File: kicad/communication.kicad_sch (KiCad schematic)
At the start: 51 parts, among them J1 CAN1A, J2 CAN1B, J3 Conn_01x02_Socket, J6 CAN1A, J7 CAN1B, U13 SK9822-EC20, U15 TJA1462ATK, U8 TJA1462ATK, U9 TJA1103AHN

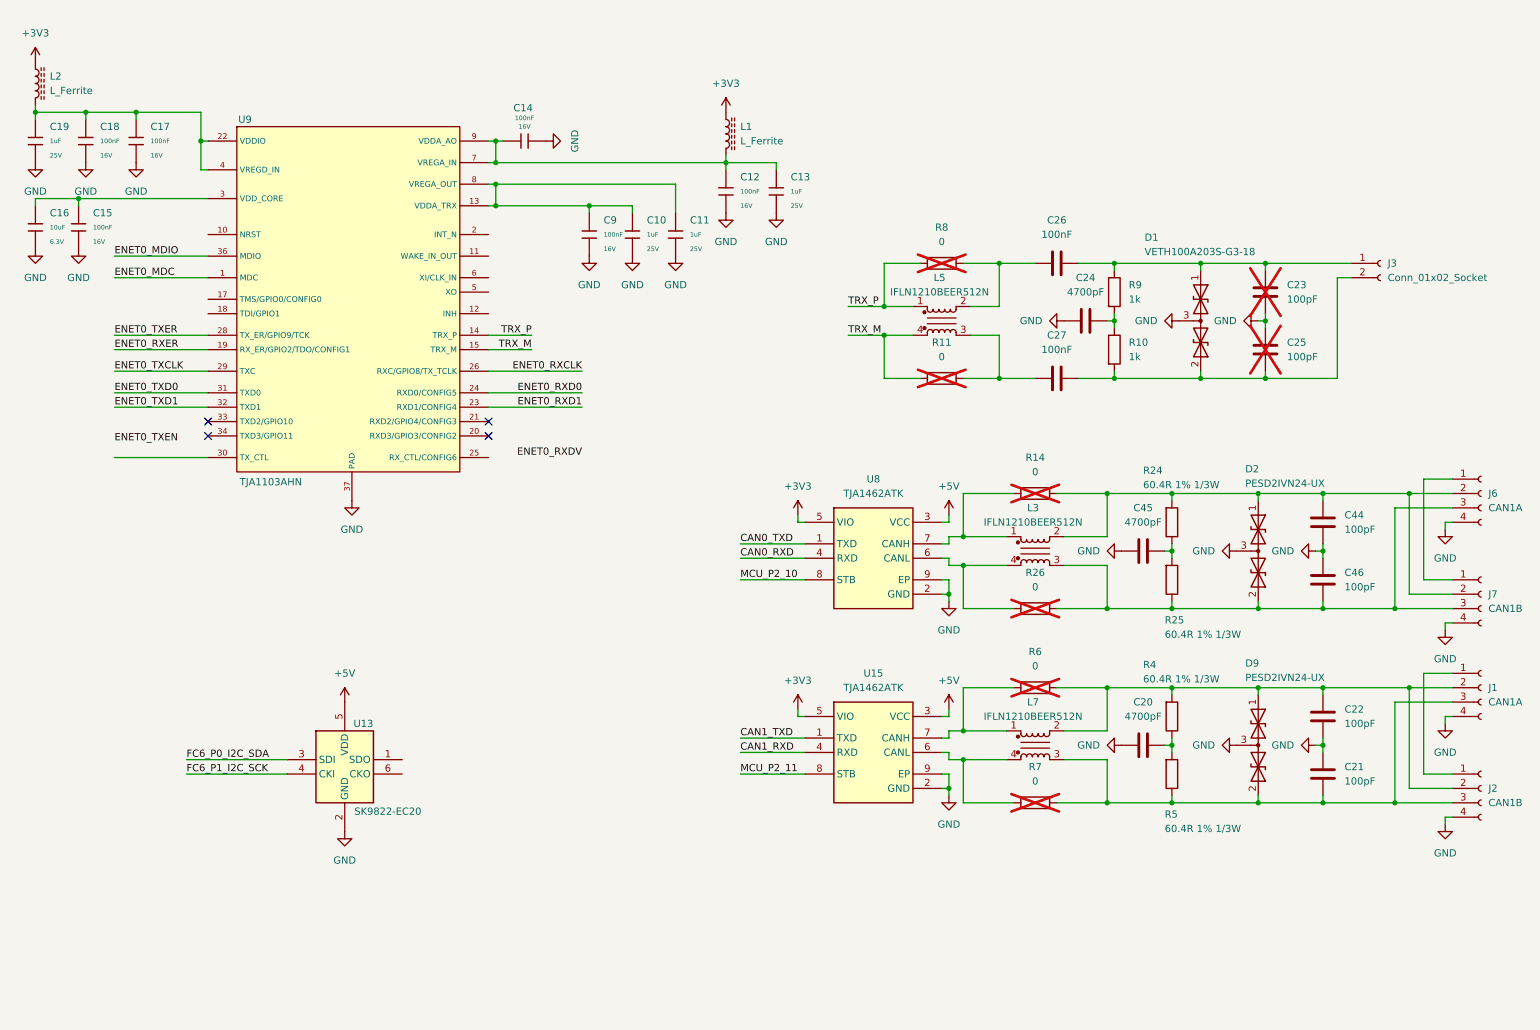
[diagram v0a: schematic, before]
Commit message: Updated schematics and BOM.
- Finished power supply schematics
- Added power schematic around MCXN
- Assigned MCXN pins
- Created board-to-board schematic and assigned pins to DF40T board-to-board connector
- Added correct sensors, finished sensor schematic
- Updated parts in communication schematic
- Added all part numbers etc in parts parameters
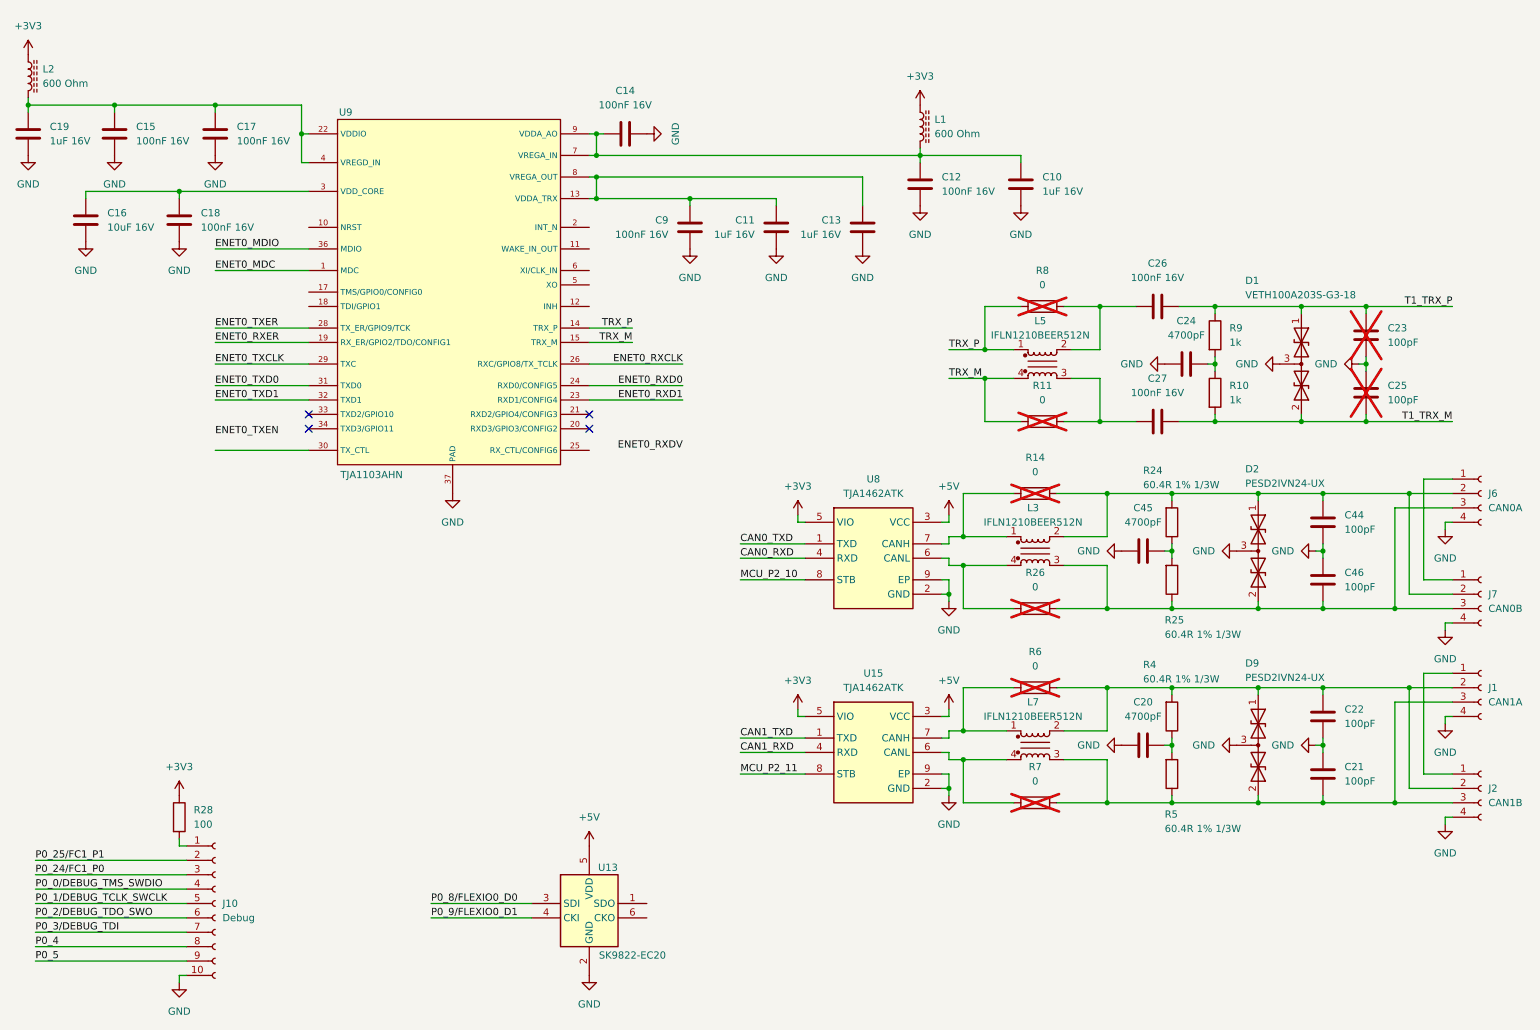
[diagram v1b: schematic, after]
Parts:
- removed C10, C11, C13, C19: 1uF, PCM_JLCPCB:C_0402, symbol PCM_JLCPCB-Capacitors:0402,1uF
- removed C12, C14, C15, C17, C18, C9: 100nF, PCM_JLCPCB:C_0402, symbol PCM_JLCPCB-Capacitors:0402,100nF
- removed C16: 10uF, PCM_JLCPCB:C_0402, symbol PCM_JLCPCB-Capacitors:0402,10uF
- removed J3: Conn_01x02_Socket, symbol Connector:Conn_01x02_Socket
- added C10, C11, C13, C19: 1uF 16V, Capacitor_SMD:C_0603_1608Metric, symbol Device:C
- added C12, C14, C15, C17, C18, C9: 100nF 16V, Capacitor_SMD:C_0402_1005Metric, symbol Device:C
- added C16: 10uF 16V, Capacitor_SMD:C_0805_2012Metric, symbol Device:C
- added J10: Debug, Connector_JST:JST_SH_SM10B-SRSS-TB_1x10-1MP_P1.00mm_Horizontal, symbol Connector:Conn_01x10_Socket
- added R28: 100, Resistor_SMD:R_0603_1608Metric, symbol Device:R
- C20, C24, C45: footprint (none) -> Capacitor_SMD:C_0402_1005Metric; MF (none) -> YAGEO; MFPN (none) -> CC0402KRX7R9BB472; Supplier (none) -> JLCPCB; Supplier PN (none) -> C106208
- C21, C22, C23, C25, C44, C46: footprint (none) -> Capacitor_SMD:C_0402_1005Metric; MF (none) -> YAGEO; MFPN (none) -> CC0402JRNPO9BN101; Supplier (none) -> JLCPCB; Supplier PN (none) -> C106200
- C26, C27: value 100nF -> 100nF 16V; footprint (none) -> Capacitor_SMD:C_0402_1005Metric; MF (none) -> Samsung Electro-Mechanics; MFPN (none) -> CL05B104KO5NNNC; Supplier (none) -> JLCPCB; Supplier PN (none) -> C1525
- D1: MF (none) -> Vishay General Semiconductor - Diodes Division; MFPN (none) -> VETH100A203S-G3-18; Supplier (none) -> DigiKey; Supplier PN (none) -> 112-VETH100A203S-G3-18CT-ND
- D2, D9: MF (none) -> Nexperia; MFPN (none) -> PESD2IVN24-UX; Supplier (none) -> JLCPCB; Supplier PN (none) -> C552496
- J1, J2: footprint (none) -> Connector_JST:JST_GH_SM04B-GHS-TB_1x04-1MP_P1.25mm_Horizontal; MF (none) -> JST; MFPN (none) -> SM04B-GHS-TB(LF)(SN); Supplier (none) -> JLCPCB; Supplier PN (none) -> C189895
- J6: value CAN1A -> CAN0A; footprint (none) -> Connector_JST:JST_GH_SM04B-GHS-TB_1x04-1MP_P1.25mm_Horizontal; MF (none) -> JST; MFPN (none) -> SM04B-GHS-TB(LF)(SN); Supplier (none) -> JLCPCB; Supplier PN (none) -> C189895
- J7: value CAN1B -> CAN0B; footprint (none) -> Connector_JST:JST_GH_SM04B-GHS-TB_1x04-1MP_P1.25mm_Horizontal; MF (none) -> JST; MFPN (none) -> SM04B-GHS-TB(LF)(SN); Supplier (none) -> JLCPCB; Supplier PN (none) -> C189895
- L1, L2: value L_Ferrite -> 600 Ohm; footprint (none) -> Inductor_SMD:L_0402_1005Metric; MF (none) -> Murata Electronics; MFPN (none) -> BLM15AG601SN1D; Supplier (none) -> JLCPCB; Supplier PN (none) -> C76884
- L3, L5, L7: MF (none) -> Vishay Dale; MFPN (none) -> IFLN1210BEER512N; Supplier (none) -> DigiKey; Supplier PN (none) -> 541-IFLN1210BEER512NCT-ND
- R10, R9: footprint (none) -> Resistor_SMD:R_0402_1005Metric; MF (none) -> UNI-ROYAL(Uniroyal Elec); MFPN (none) -> 0402WGF1001TCE; Supplier (none) -> JLCPCB; Supplier PN (none) -> C11702
- R11, R14, R26, R6, R7, R8: footprint (none) -> Resistor_SMD:R_0402_1005Metric; MF (none) -> UNI-ROYAL(Uniroyal Elec); MFPN (none) -> 0402WGF0000TCE; Supplier (none) -> JLCPCB; Supplier PN (none) -> C17168
- R24, R25, R4, R5: MF (none) -> Vishay Dale; MFPN (none) -> CRCW060360R4FKEAHP; Supplier (none) -> DigiKey; Supplier PN (none) -> 541-60.4SCT-ND
- U13: footprint SK9822EC20 -> RGB_leds:SK9822EC20; MF (none) -> OPSCO Optoelectronics; MFPN (none) -> SK9822-EC20; Supplier (none) -> JLCPCB; Supplier PN (none) -> C2909059
- U15, U8: MF (none) -> NXP Semicon; MFPN (none) -> TJA1462ATK/0Z; Supplier (none) -> JLCPCB; Supplier PN (none) -> C3229259
- U9: MF (none) -> NXP USA Inc.; MFPN (none) -> TJA1103AHN/0Z; Supplier (none) -> DigiKey; Supplier PN (none) -> 568-TJA1103AHN/0ZCT-ND
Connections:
- net +3V3: now also R28.1
- net GND: now also C10.1, C11.1, C12.1, C13.1, C14.2, C15.1, C16.1, C17.1, C18.1, C19.1, C9.1, J10.10 (Pin_10)
- net VDDA_TRX: now also C11.2, C13.2, C9.2
- net VDDIO: now also C15.2, C17.2, C19.2
- net at U9.3 (VDD_CORE): now also C16.2, C18.2
- net at L1.2, U9.7 (VREGA_IN), U9.9 (VDDA_AO): now also C10.2, C12.2, C14.1
- net T1_TRX_P: now reaches C23.2, C26.2, D1.1 (A1), R9.1
- net T1_TRX_M: now reaches C25.1, C27.2, D1.2 (A2), R10.2
- net FC6_P0_I2C_SDA renamed P0_8/FLEXIO0_D0
- net FC6_P1_I2C_SCK renamed P0_9/FLEXIO0_D1
- new net: J10.1 (Pin_1), R28.2
- new net P0_0/DEBUG_TMS_SWDIO: J10.4 (Pin_4)
- new net P0_1/DEBUG_TCLK_SWCLK: J10.5 (Pin_5)
- new net P0_24/FC1_P0: J10.3 (Pin_3)
- new net P0_25/FC1_P1: J10.2 (Pin_2)
- new net P0_2/DEBUG_TDO_SWO: J10.6 (Pin_6)
- new net P0_3/DEBUG_TDI: J10.7 (Pin_7)
- new net P0_4: J10.8 (Pin_8)
- new net P0_5: J10.9 (Pin_9)
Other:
- moved on the sheet: C23, C24, C25, C26, C27, D1, L1, L2, L5, R10, R11, R8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

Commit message: Finished schematic design for first review
Finished schematic design for first review.
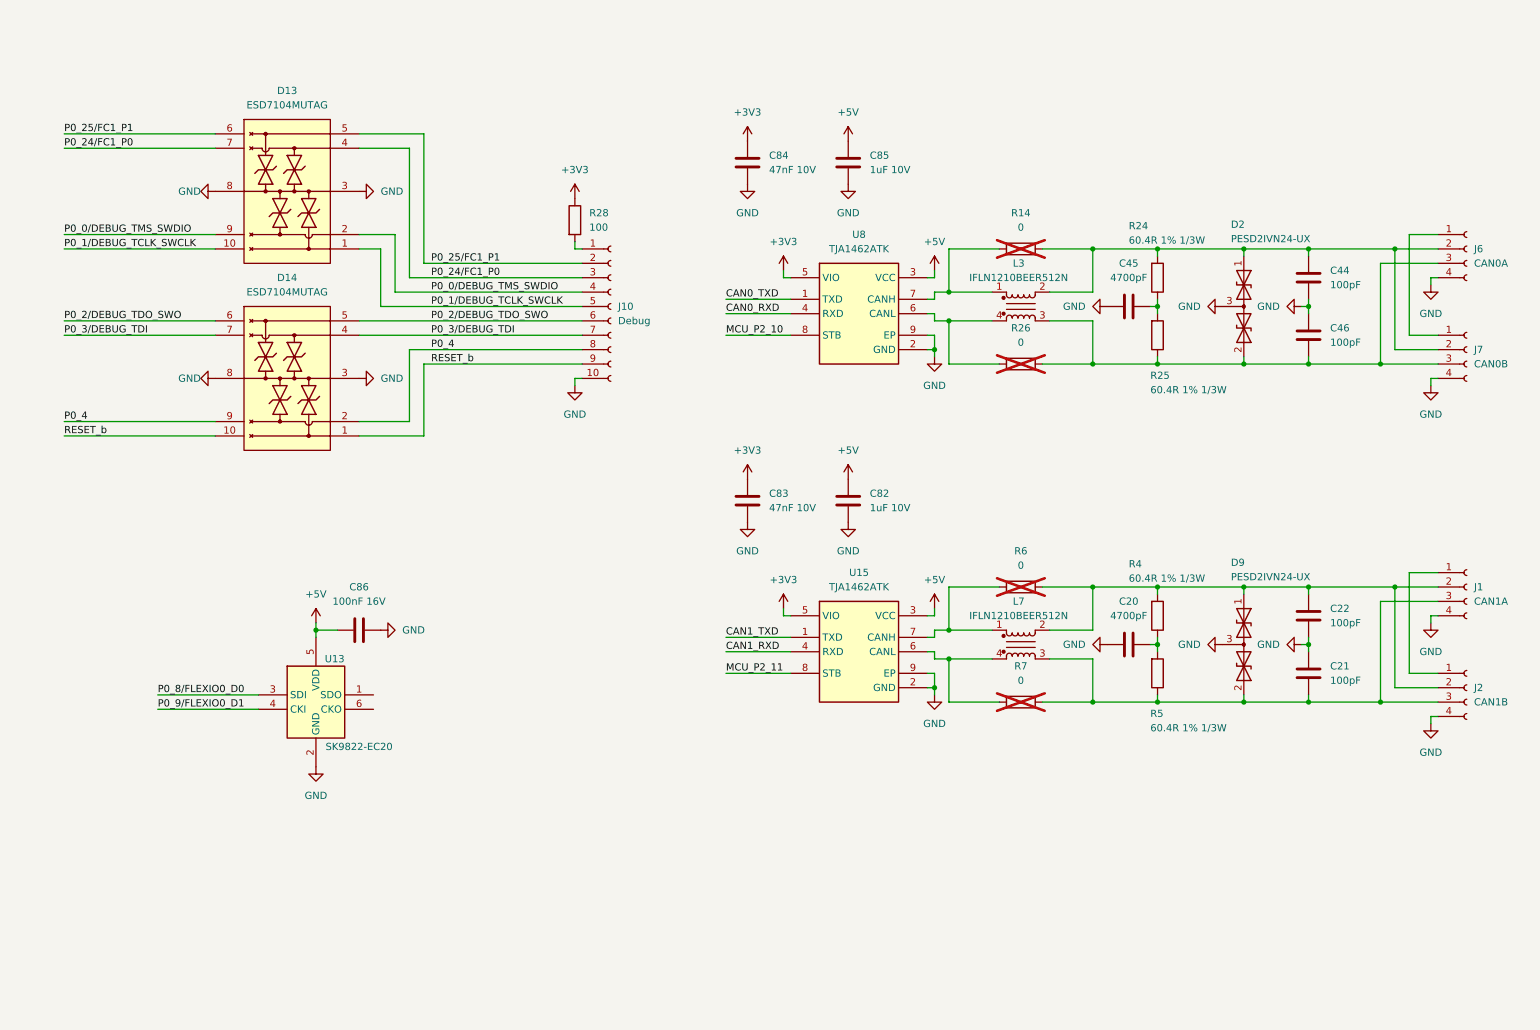
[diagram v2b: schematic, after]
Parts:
- removed C10, C11, C13, C19: 1uF 16V, Capacitor_SMD:C_0603_1608Metric, symbol Device:C
- removed C12, C14, C15, C17, C18, C26, C27, C9: 100nF 16V, Capacitor_SMD:C_0402_1005Metric, symbol Device:C
- removed C16: 10uF 16V, Capacitor_SMD:C_0805_2012Metric, symbol Device:C
- removed C23, C25: 100pF, Capacitor_SMD:C_0402_1005Metric, symbol Device:C
- removed C24: 4700pF, Capacitor_SMD:C_0402_1005Metric, symbol Device:C
- removed D1: VETH100A203S-G3-18, Package_TO_SOT_SMD:SOT-23, symbol Diodes:VETH100A203S-G3-18
- removed L1, L2: 600 Ohm, Inductor_SMD:L_0402_1005Metric, symbol Device:L_Ferrite
- removed L5: IFLN1210BEER512N, Inductors:IFLN1210BEER512N, symbol Inductors:IFLN1210BEER512N
- removed R10, R9: 1k, Resistor_SMD:R_0402_1005Metric, symbol Device:R
- removed R11, R8: 0, Resistor_SMD:R_0402_1005Metric, symbol Device:R
- removed U9: TJA1103AHN, NXP_HV:HVQFN36_SOT1092-2_NXP, symbol Transceivers:TJA1103AHN
- added C82, C85: 1uF 10V, Capacitor_SMD:C_0603_1608Metric, symbol Device:C
- added C83, C84: 47nF 10V, Capacitor_SMD:C_0402_1005Metric, symbol Device:C
- added C86: 100nF 16V, Capacitor_SMD:C_0402_1005Metric, symbol Device:C
- added D13, D14: ESD7104MUTAG, TVS:ESD8104MUTAG, symbol TVS:ESD7104MUTAG
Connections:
- net +3V3: now also C83.1, C84.1
- net +5V: now also C82.1, C85.1, C86.1
- net GND: now also C82.2, C83.2, C84.2, C85.2, C86.2, D13.3 (GND_1), D13.8 (GND_2), D14.3 (GND_1), D14.8 (GND_2)
- net P0_0/DEBUG_TMS_SWDIO: now also D13.2 (IO_2), D13.9 (NC_3)
- net P0_1/DEBUG_TCLK_SWCLK: now also D13.1 (IO_1), D13.10 (NC_4)
- net P0_24/FC1_P0: now also D13.4 (IO_3), D13.7 (NC_2)
- net P0_25/FC1_P1: now also D13.5 (IO_4), D13.6 (NC_1)
- net P0_2/DEBUG_TDO_SWO: now also D14.5 (IO_4), D14.6 (NC_1)
- net P0_3/DEBUG_TDI: now also D14.4 (IO_3), D14.7 (NC_2)
- net P0_4: now also D14.2 (IO_2), D14.9 (NC_3)
- net P0_5 renamed RESET_b
- net RESET_b: now also D14.1 (IO_1), D14.10 (NC_4)
- no-connect marks 4 -> 0
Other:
- moved on the sheet: C20, C21, C22, C44, C45, C46, D2, D9, J1, J10, J2, J6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
